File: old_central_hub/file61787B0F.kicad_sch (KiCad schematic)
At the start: 49 parts, among them J201 Conn_01x04, J202 Conn_01x04, J203 Conn_02x05_Odd_Even, J204 Conn_02x05_Odd_Even, J205 Conn_01x04, J206 Conn_02x05_Odd_Even

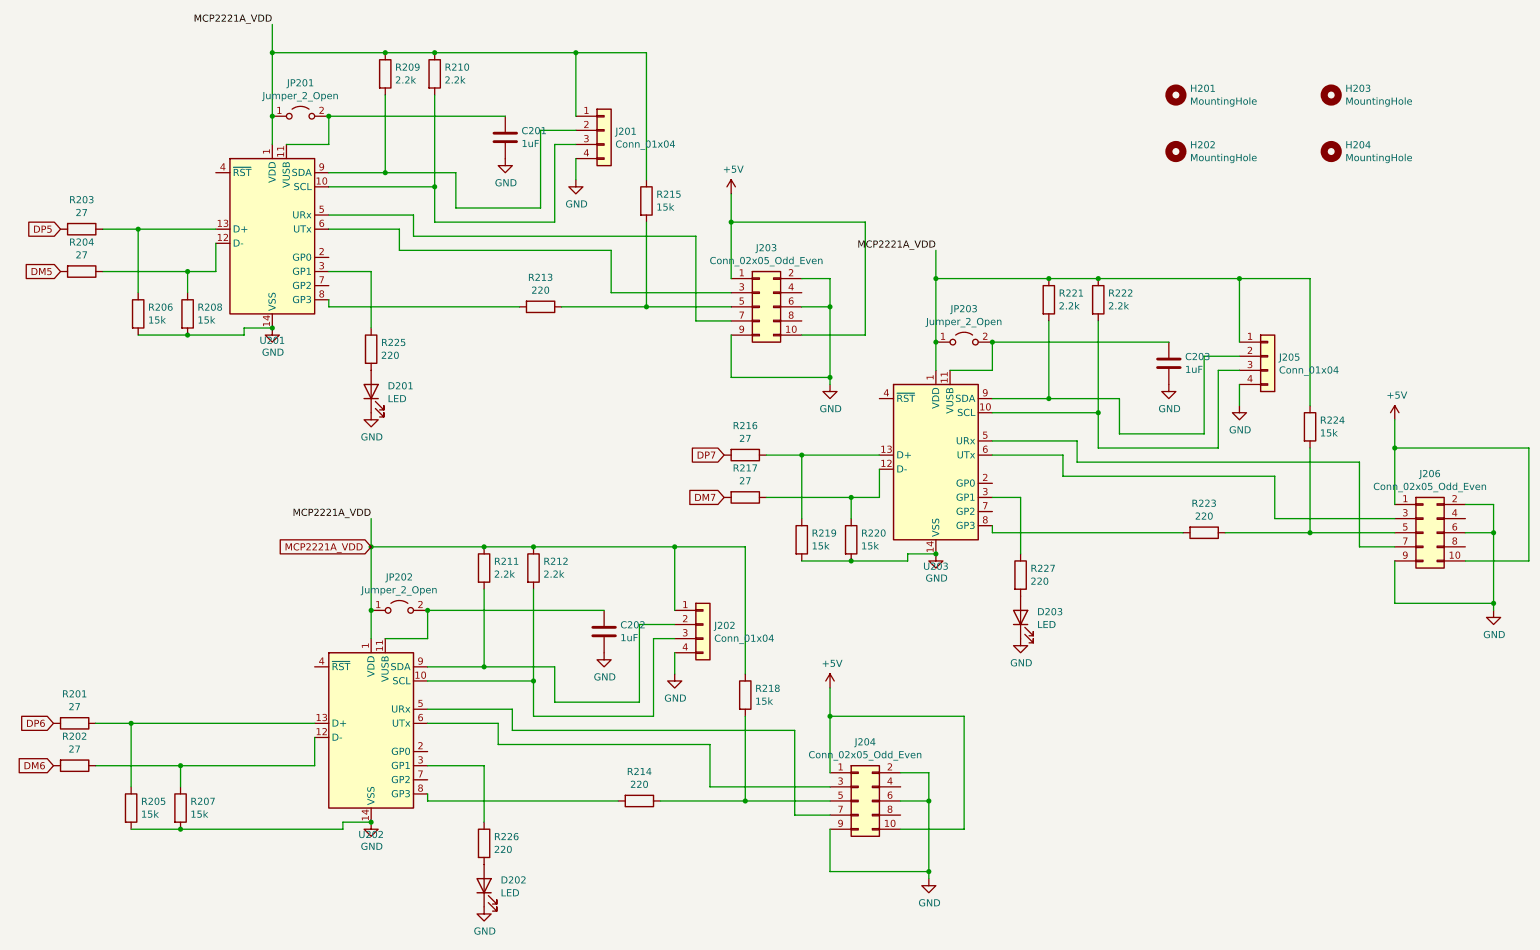
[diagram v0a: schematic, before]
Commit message: Add 12V->5V converter
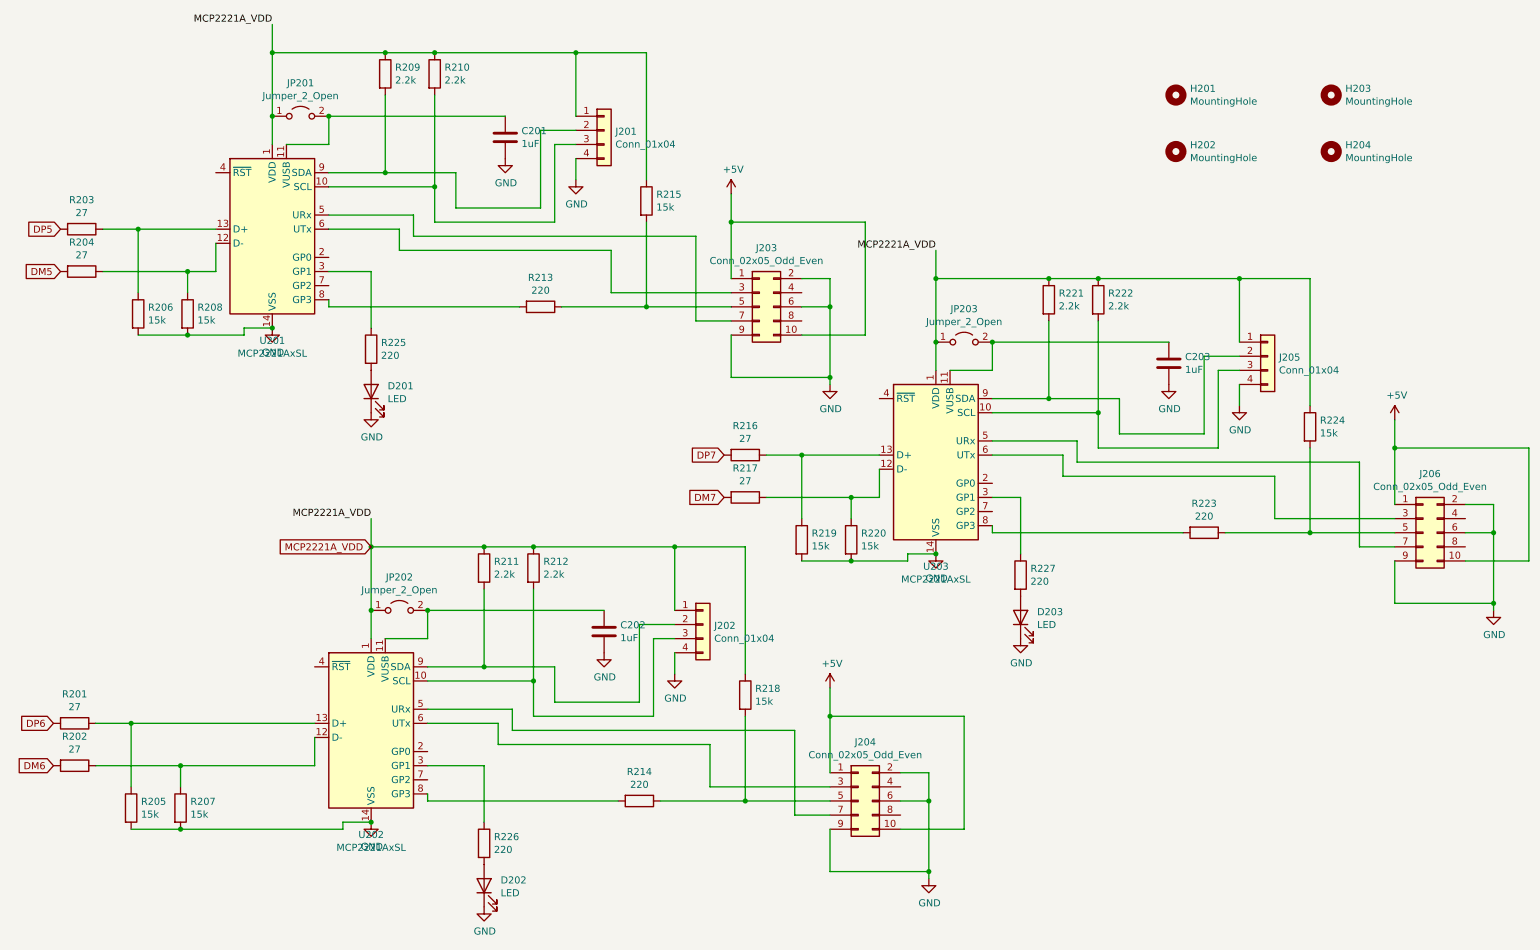
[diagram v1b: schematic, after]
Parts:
- U201, U202, U203: value (none) -> MCP2221AxSL
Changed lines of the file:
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@@
     (in_bom yes) (on_board yes)
     (property "Reference" "U201" (id 0) (at 55.88 75.9206 0))
-    (property "Value" "" (id 1) (at 55.88 78.232 0))
+    (property "Value" "MCP2221AxSL" (id 1) (at 55.88 78.232 0))
     (property "Footprint" "" (id 2) (at 55.88 33.02 0)
       (effects (font (size 1.27 1.27)) hide)
@@
     (in_bom yes) (on_board yes)
     (property "Reference" "U202" (id 0) (at 73.66 164.8206 0))
-    (property "Value" "" (id 1) (at 73.66 167.132 0))
+    (property "Value" "MCP2221AxSL" (id 1) (at 73.66 167.132 0))
     (property "Footprint" "" (id 2) (at 73.66 121.92 0)
       (effects (font (size 1.27 1.27)) hide)
@@
     (in_bom yes) (on_board yes)
     (property "Reference" "U203" (id 0) (at 175.26 116.5606 0))
-    (property "Value" "" (id 1) (at 175.26 118.872 0))
+    (property "Value" "MCP2221AxSL" (id 1) (at 175.26 118.872 0))
     (property "Footprint" "" (id 2) (at 175.26 73.66 0)
       (effects (font (size 1.27 1.27)) hide)
